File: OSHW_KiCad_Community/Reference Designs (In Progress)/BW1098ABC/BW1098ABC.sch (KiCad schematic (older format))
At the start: 10 parts

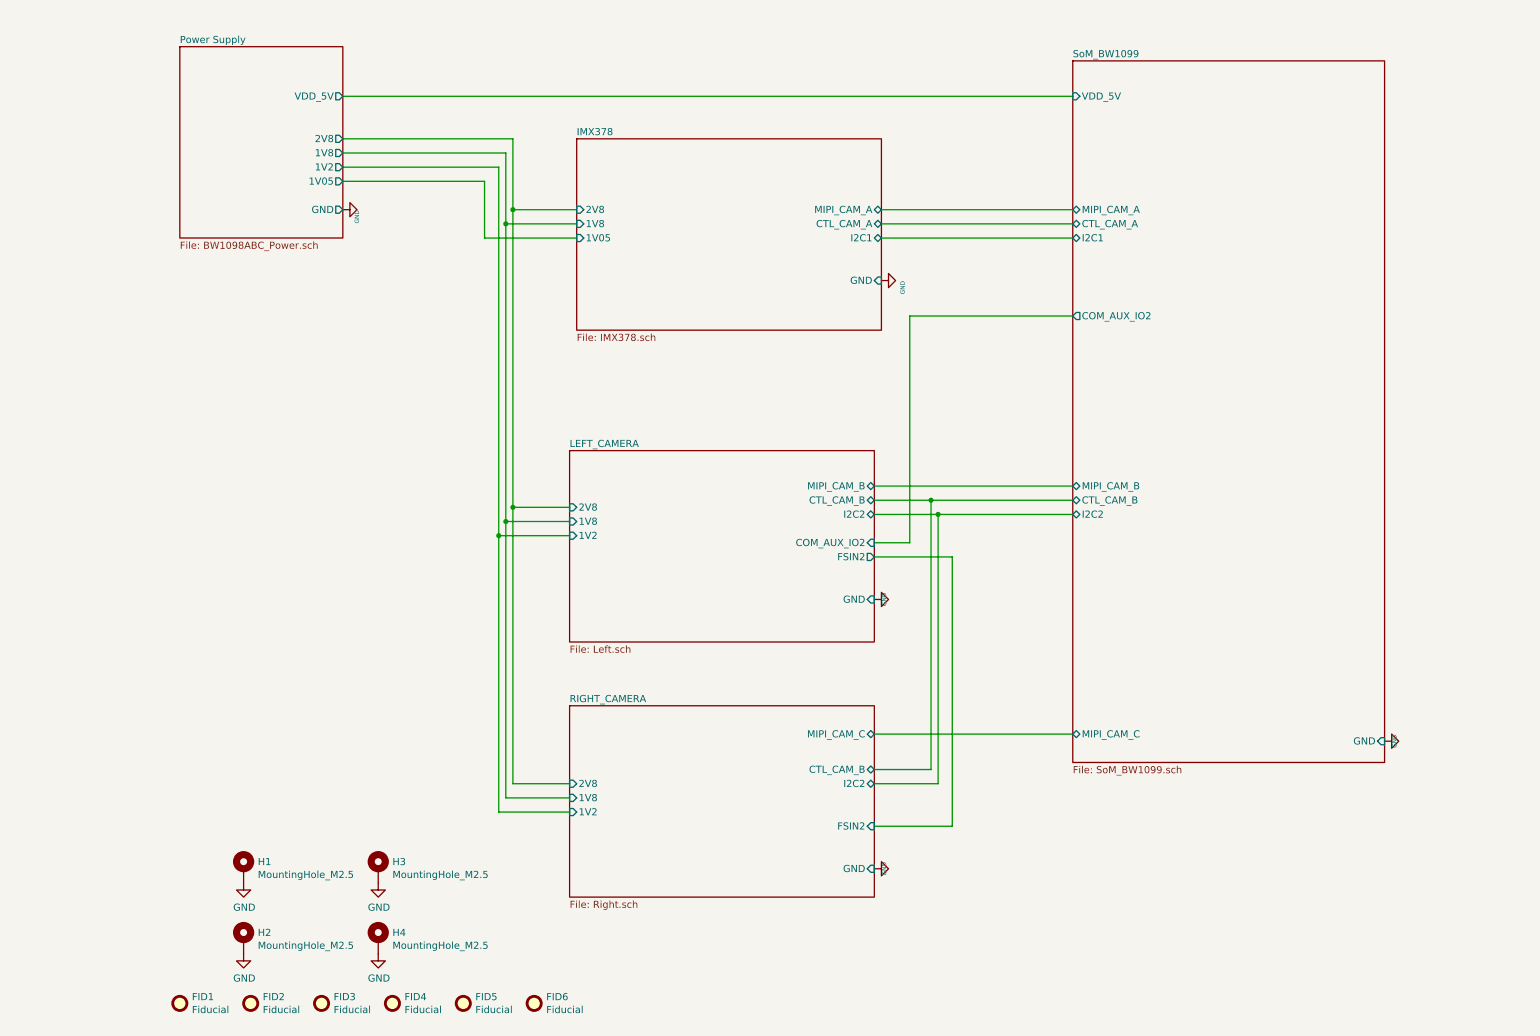
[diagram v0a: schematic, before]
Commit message: BW1098ABC - added back in usbc, got rid of hierarchical labeling in favor of globals. Passes ERC
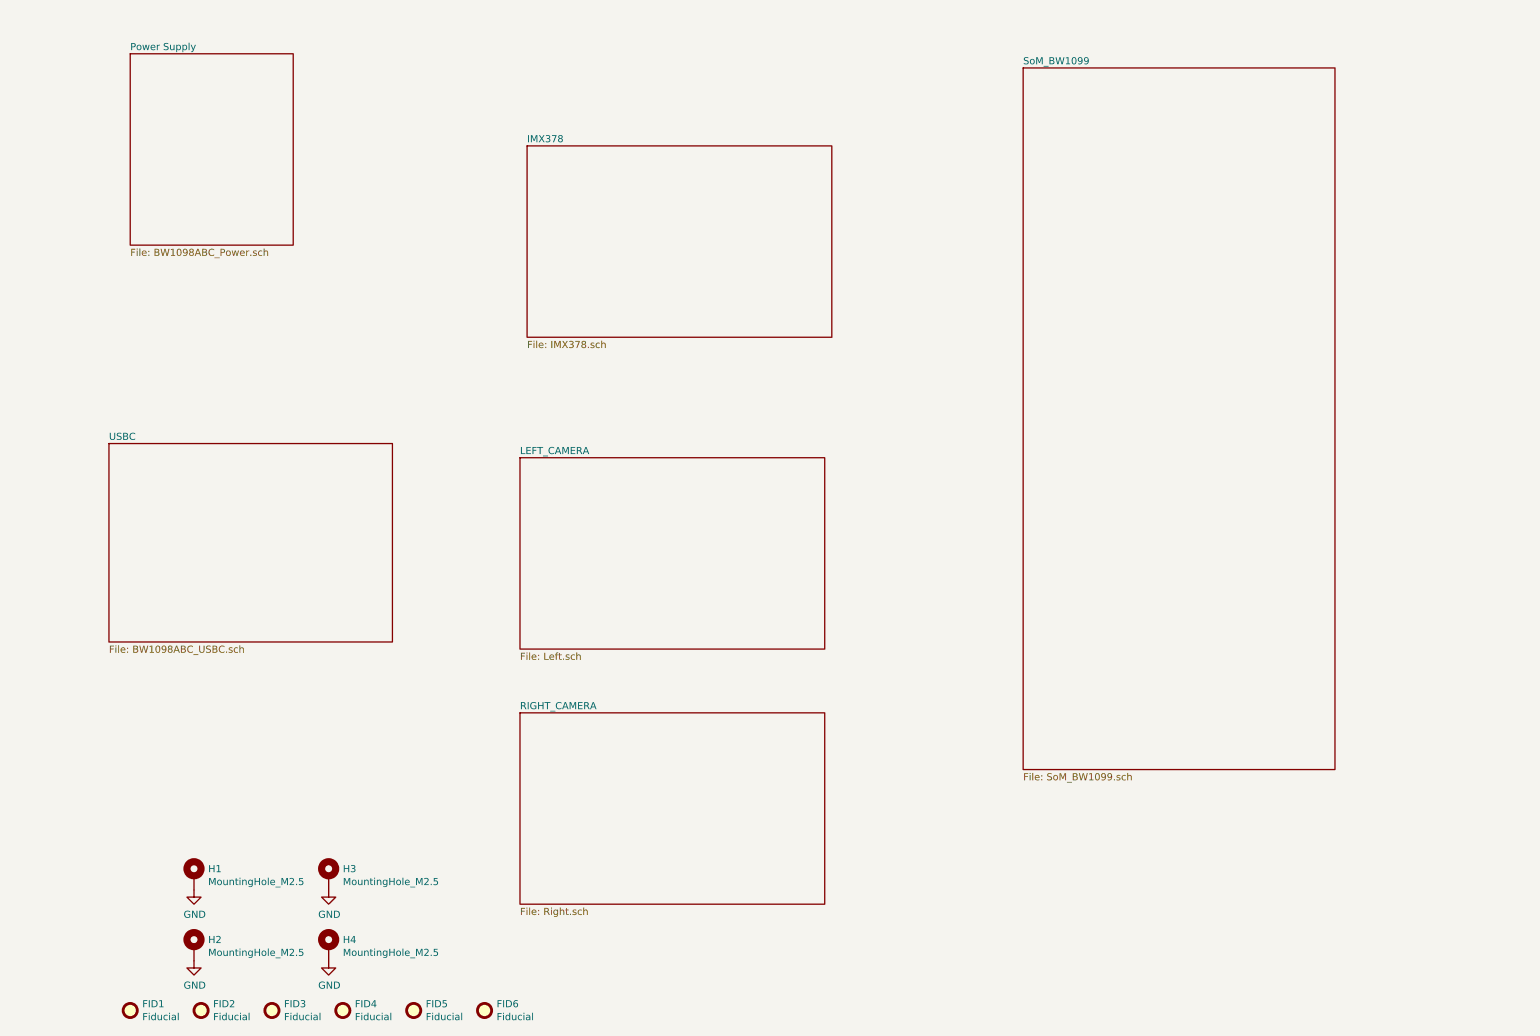
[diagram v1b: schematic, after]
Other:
- moved on the sheet: FID1, FID2, FID3, FID4, FID5

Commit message: going through footprints and datasheet stuff
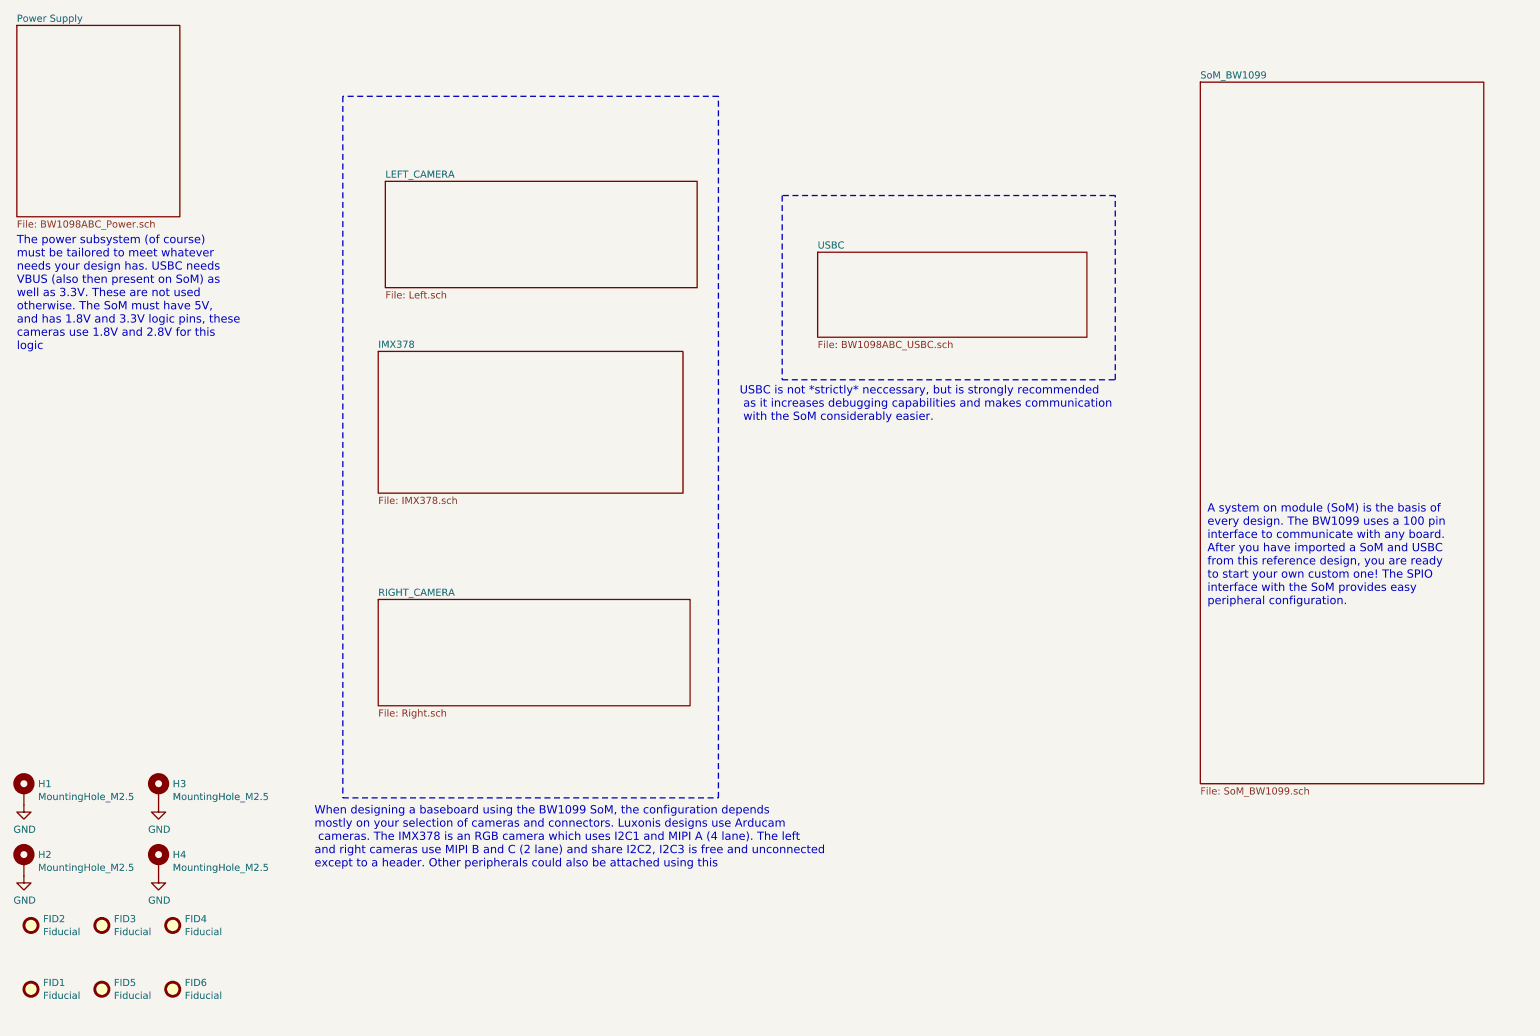
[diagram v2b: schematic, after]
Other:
- note added: "A system on module (SoM) is the basis of \nevery design. The BW1099 uses a 100 pin\ninterface to communicate with any board. \nAfter you have imported a SoM and USBC\nfrom this reference design, you are ready \nto start your own custom one! The SPIO \ninterface with the SoM provides easy \nperipheral configuration."
- note added: "The power subsystem (of course)\nmust be tailored to meet whatever\nneeds your design has. USBC needs\nVBUS (also then present on SoM) as \nwell as 3.3V. These are not used \notherwise. The SoM must have 5V, \nand has 1.8V and 3.3V logic pins, these \ncameras use 1.8V and 2.8V for this \nlogic"
- note added: "USBC is not *strictly* neccessary, but is strongly recommended\n as it increases debugging capabilities and makes communication\n with the SoM considerably easier.\n"
- note added: "When designing a baseboard using the BW1099 SoM, the configuration depends \nmostly on your selection of cameras and connectors. Luxonis designs use Arducam\n cameras. The IMX378 is an RGB camera which uses I2C1 and MIPI A (4 lane). The left \nand right cameras use MIPI B and C (2 lane) and share I2C2, I2C3 is free and unconnected \nexcept to a header. Other peripherals could also be attached usi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"
- moved on the sheet: FID1, FID2, FID3, FID4, FID5, FID6, H1, H2, H3, H4
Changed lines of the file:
@@
 $EndDescr
 $Sheet
-S 7700 900  2200 4950
+S 8950 1000 2000 4950
 U 5FF8D9B2
 F0 "SoM_BW1099" 50
@@
 $EndSheet
 $Sheet
-S 4150 5450 2150 1350
+S 3150 4650 2200 750
 U 5FF8D40A
 F0 "RIGHT_CAMERA" 50
@@
 L Mechanical:Fiducial FID1
 U 1 1 6049A903
-P 1400 7550
-F 0 "FID1" H 1485 7596 50  0000 L CNN
-F 1 "Fiducial" H 1485 7505 50  0000 L CNN
-F 2 "Fiducial:Fiducial_1mm_Mask2mm" H 1400 7550 50  0001 C CNN
-F 3 "~" H 1400 7550 50  0001 C CNN
-	1    1400 7550
+P 700 7400
+F 0 "FID1" H 785 7446 50  0000 L CNN
+F 1 "Fiducial" H 785 7355 50  0000 L CNN
+F 2 "Fiducial:Fiducial_1mm_Mask2mm" H 700 7400 50  0001 C CNN
+F 3 "~" H 700 7400 50  0001 C CNN
+	1    700  7400
 	1    0    0    -1
 $EndComp
@@
 L Mechanical:Fiducial FID2
 U 1 1 5FF51DEB
-P 1900 7550
-F 0 "FID2" H 1985 7596 50  0000 L CNN
-F 1 "Fiducial" H 1985 7505 50  0000 L CNN
-F 2 "Fiducial:Fiducial_1mm_Mask2mm" H 1900 7550 50  0001 C CNN
-F 3 "~" H 1900 7550 50  0001 C CNN
-	1    1900 7550
+P 700 6950
+F 0 "FID2" H 785 6996 50  0000 L CNN
+F 1 "Fiducial" H 785 6905 50  0000 L CNN
+F 2 "Fiducial:Fiducial_1mm_Mask2mm" H 700 6950 50  0001 C CNN
+F 3 "~" H 700 6950 50  0001 C CNN
+	1    700  6950
 	1    0    0    -1
 $EndComp
@@
 L Mechanical:Fiducial FID3
 U 1 1 6049A905
-P 2400 7550
-F 0 "FID3" H 2485 7596 50  0000 L CNN
-F 1 "Fiducial" H 2485 7505 50  0000 L CNN
-F 2 "Fiducial:Fiducial_1mm_Mask2mm" H 2400 7550 50  0001 C CNN
-F 3 "~" H 2400 7550 50  0001 C CNN
-	1    2400 7550
+P 1200 6950
+F 0 "FID3" H 1285 6996 50  0000 L CNN
+F 1 "Fiducial" H 1285 6905 50  0000 L CNN
+F 2 "Fiducial:Fiducial_1mm_Mask2mm" H 1200 6950 50  0001 C CNN
+F 3 "~" H 1200 6950 50  0001 C CNN
+	1    1200 6950
 	1    0    0    -1
 $EndComp
@@
 L Mechanical:Fiducial FID4
 U 1 1 6049A906
-P 2900 7550
-F 0 "FID4" H 2985 7596 50  0000 L CNN
-F 1 "Fiducial" H 2985 7505 50  0000 L CNN
-F 2 "Fiducial:Fiducial_1mm_Mask2mm" H 2900 7550 50  0001 C CNN
-F 3 "~" H 2900 7550 50  0001 C CNN
-	1    2900 7550
+P 1700 6950
+F 0 "FID4" H 1785 6996 50  0000 L CNN
+F 1 "Fiducial" H 1785 6905 50  0000 L CNN
+F 2 "Fiducial:Fiducial_1mm_Mask2mm" H 1700 6950 50  0001 C CNN
+F 3 "~" H 1700 6950 50  0001 C CNN
+	1    1700 6950
 	1    0    0    -1
 $EndComp
@@
 L Mechanical:Fiducial FID5
 U 1 1 6049A907
-P 3400 7550
-F 0 "FID5" H 3485 7596 50  0000 L CNN
-F 1 "Fiducial" H 3485 7505 50  0000 L CNN
-F 2 "Fiducial:Fiducial_1mm_Mask2mm" H 3400 7550 50  0001 C CNN
-F 3 "~" H 3400 7550 50  0001 C CNN
-	1    3400 7550
+P 1200 7400
+F 0 "FID5" H 1285 7446 50  0000 L CNN
+F 1 "Fiducial" H 1285 7355 50  0000 L CNN
+F 2 "Fiducial:Fiducial_1mm_Mask2mm" H 1200 7400 50  0001 C CNN
+F 3 "~" H 1200 7400 50  0001 C CNN
+	1    1200 7400
 	1    0    0    -1
 $EndComp
@@
 L Mechanical:Fiducial FID6
 U 1 1 600C0C22
-P 3900 7550
-F 0 "FID6" H 3985 7596 50  0000 L CNN
-F 1 "Fiducial" H 3985 7505 50  0000 L CNN
-F 2 "Fiducial:Fiducial_1mm_Mask2mm" H 3900 7550 50  0001 C CNN
-F 3 "~" H 3900 7550 50  0001 C CNN
-	1    3900 7550
+P 1700 7400
+F 0 "FID6" H 1785 7446 50  0000 L CNN
+F 1 "Fiducial" H 1785 7355 50  0000 L CNN
+F 2 "Fiducial:Fiducial_1mm_Mask2mm" H 1700 7400 50  0001 C CNN
+F 3 "~" H 1700 7400 50  0001 C CNN
+	1    1700 7400
 	1    0    0    -1
 $EndComp
@@
 L BW1098ABC-rescue:Mechanical_MountingHole_Pad-depthAI_sch H1
 U 1 1 600C0C23
-P 1850 6600
-F 0 "H1" H 1950 6649 50  0000 L CNN
-F 1 "MountingHole_M2.5" H 1950 6558 50  0000 L CNN
-F 2 "fp_luxonis:Mounting_Wuerth_WA-SMSI-M2_H3mm_9774030243" H 1850 6600 50  0001 C CNN
-F 3 "" H 1850 6600 50  0001 C CNN
-	1    1850 6600
+P 650 6000
+F 0 "H1" H 750 6049 50  0000 L CNN
+F 1 "MountingHole_M2.5" H 750 5958 50  0000 L CNN
+F 2 "fp_luxonis:Mounting_Wuerth_WA-SMSI-M2_H3mm_9774030243" H 650 6000 50  0001 C CNN
+F 3 "" H 650 6000 50  0001 C CNN
+	1    650  6000
 	1    0    0    -1
 $EndComp
@@
 L BW1098ABC-rescue:Mechanical_MountingHole_Pad-depthAI_sch H2
 U 1 1 600C0C24
-P 1850 7100
-F 0 "H2" H 1950 7149 50  0000 L CNN
-F 1 "MountingHole_M2.5" H 1950 7058 50  0000 L CNN
-F 2 "fp_luxonis:Mounting_Wuerth_WA-SMSI-M2_H3mm_9774030243" H 1850 7100 50  0001 C CNN
-F 3 "" H 1850 7100 50  0001 C CNN
-	1    1850 7100
+P 650 6500
+F 0 "H2" H 750 6549 50  0000 L CNN
+F 1 "MountingHole_M2.5" H 750 6458 50  0000 L CNN
+F 2 "fp_luxonis:Mounting_Wuerth_WA-SMSI-M2_H3mm_9774030243" H 650 6500 50  0001 C CNN
+F 3 "" H 650 6500 50  0001 C CNN
+	1    650  6500
 	1    0    0    -1
 $EndComp
@@
 L BW1098ABC-rescue:Mechanical_MountingHole_Pad-depthAI_sch H4
 U 1 1 600C0C25
-P 2800 7100
-F 0 "H4" H 2900 7149 50  0000 L CNN
-F 1 "MountingHole_M2.5" H 2900 7058 50  0000 L CNN
-F 2 "fp_luxonis:Mounting_Wuerth_WA-SMSI-M2_H3mm_9774030243" H 2800 7100 50  0001 C CNN
-F 3 "" H 2800 7100 50  0001 C CNN
-	1    2800 7100
+P 1600 6500
+F 0 "H4" H 1700 6549 50  0000 L CNN
+F 1 "MountingHole_M2.5" H 1700 6458 50  0000 L CNN
+F 2 "fp_luxonis:Mounting_Wuerth_WA-SMSI-M2_H3mm_9774030243" H 1600 6500 50  0001 C CNN
+F 3 "" H 1600 6500 50  0001 C CNN
+	1    1600 6500
 	1    0    0    -1
 $EndComp
@@
 L BW1098ABC-rescue:Mechanical_MountingHole_Pad-depthAI_sch H3
 U 1 1 600C0C26
-P 2800 6600
-F 0 "H3" H 2900 6649 50  0000 L CNN
-F 1 "MountingHole_M2.5" H 2900 6558 50  0000 L CNN
-F 2 "fp_luxonis:Mounting_Wuerth_WA-SMSI-M2_H3mm_9774030243" H 2800 6600 50  0001 C CNN
-F 3 "" H 2800 6600 50  0001 C CNN
-	1    2800 6600
-	1    0    0    -1
-$EndComp
-$Sheet
-S 1400 800  1150 1350
+P 1600 6000
+F 0 "H3" H 1700 6049 50  0000 L CNN
+F 1 "MountingHole_M2.5" H 1700 5958 50  0000 L CNN
+F 2 "fp_luxonis:Mounting_Wuerth_WA-SMSI-M2_H3mm_9774030243" H 1600 6000 50  0001 C CNN
+F 3 "" H 1600 6000 50  0001 C CNN
+	1    1600 6000
+	1    0    0    -1
+$EndComp
+$Sheet
+S 600  600  1150 1350
 U 604AEAFA
 F0 "Power Supply" 50
@@
 $EndSheet
 $Sheet
-S 4200 1450 2150 1350
+S 3150 2900 2150 1000
 U 5FF8D4A5
 F0 "IMX378" 50
@@
 $EndSheet
 $Sheet
-S 4150 3650 2150 1350
+S 3200 1700 2200 750
 U 5FF8D2B3
 F0 "LEFT_CAMERA" 50
@@
 L power:GND #PWR0107
 U 1 1 6106C817
-P 1850 6700
-F 0 "#PWR0107" H 1850 6450 50  0001 C CNN
-F 1 "GND" H 1855 6527 50  0000 C CNN
-F 2 "" H 1850 6700 50  0001 C CNN
-F 3 "" H 1850 6700 50  0001 C CNN
-	1    1850 6700
+P 650 6100
+F 0 "#PWR0107" H 650 5850 50  0001 C CNN
+F 1 "GND" H 655 5927 50  0000 C CNN
+F 2 "" H 650 6100 50  0001 C CNN
+F 3 "" H 650 6100 50  0001 C CNN
+	1    650  6100
 	1    0    0    -1
 $EndComp
@@
 L power:GND #PWR0108
 U 1 1 6106D903
-P 2800 6700
-F 0 "#PWR0108" H 2800 6450 50  0001 C CNN
-F 1 "GND" H 2805 6527 50  0000 C CNN
-F 2 "" H 2800 6700 50  0001 C CNN
-F 3 "" H 2800 6700 50  0001 C CNN
-	1    2800 6700
+P 1600 6100
+F 0 "#PWR0108" H 1600 5850 50  0001 C CNN
+F 1 "GND" H 1605 5927 50  0000 C CNN
+F 2 "" H 1600 6100 50  0001 C CNN
+F 3 "" H 1600 6100 50  0001 C CNN
+	1    1600 6100
 	1    0    0    -1
 $EndComp
@@
 L power:GND #PWR0109
 U 1 1 6106E6FC
-P 2800 7200
-F 0 "#PWR0109" H 2800 6950 50  0001 C CNN
-F 1 "GND" H 2805 7027 50  0000 C CNN
-F 2 "" H 2800 7200 50  0001 C CNN
-F 3 "" H 2800 7200 50  0001 C CNN
-	1    2800 7200
+P 1600 6600
+F 0 "#PWR0109" H 1600 6350 50  0001 C CNN
+F 1 "GND" H 1605 6427 50  0000 C CNN
+F 2 "" H 1600 6600 50  0001 C CNN
+F 3 "" H 1600 6600 50  0001 C CNN
+	1    1600 6600
 	1    0    0    -1
 $EndComp
@@
 L power:GND #PWR0110
 U 1 1 6106EA7D
-P 1850 7200
-F 0 "#PWR0110" H 1850 6950 50  0001 C CNN
-F 1 "GND" H 1855 7027 50  0000 C CNN
-F 2 "" H 1850 7200 50  0001 C CNN
-F 3 "" H 1850 7200 50  0001 C CNN
-	1    1850 7200
-	1    0    0    -1
-$EndComp
-$Sheet
-S 1250 3550 2000 1400
+P 650 6600
+F 0 "#PWR0110" H 650 6350 50  0001 C CNN
+F 1 "GND" H 655 6427 50  0000 C CNN
+F 2 "" H 650 6600 50  0001 C CNN
+F 3 "" H 650 6600 50  0001 C CNN
+	1    650  6600
+	1    0    0    -1
+$EndComp
+$Sheet
+S 6250 2200 1900 600
 U 60483E6B
 F0 "USBC" 50
 F1 "BW1098ABC_USBC.sch" 50
 $EndSheet
+Wire Notes Line
+	5550 1100 2900 1100
+Wire Notes Line
+	2900 1100 2900 6050
+Wire Notes Line
+	2900 6050 5550 6050
+Wire Notes Line
+	5550 6050 5550 1100
+Text Notes 2700 6550 0    58   ~ 0
+When designing a baseboard using the BW1099 SoM, the configuration depends \nmostly on your selection of cameras and connectors. Luxonis designs use Arducam\n cameras. The IMX378 is an RGB camera which uses I2C1 and MIPI A (4 lane). The left \nand right cameras use MIPI B and C (2 lane) and share I2C2, I2C3 is free and unconnected \nexcept to a header. Other peripherals could also be attached using this\n
+Wire Notes Line
+	8350 1800 6000 1800
+Wire Notes Line
+	6000 1800 6000 3100
+Wire Notes Line
+	6000 3100 8350 3100
+Wire Notes Line
+	8350 3100 8350 1800
+Text Notes 5700 3400 0    58   ~ 0
+USBC is not *strictly* neccessary, but is strongly recommended\n as it increases debugging capabilities and makes communication\n with the SoM considerably easier.\n
+Text Notes 9000 4700 0    58   ~ 0
+A system on module (SoM) is the basis of \nevery design. The BW1099 uses a 100 pin\ninterface to communicate with any board. \nAfter you have imported a SoM and USBC\nfrom this reference design, you are ready \nto start your own custom one! The SPIO \ninterface with the SoM provides easy \nperipheral configuration.
+Text Notes 600  2900 0    58   ~ 0
+The power subsystem (of course)\nmust be tailored to meet whatever\nneeds your design has. USBC needs\nVBUS (also then present on SoM) as \nwell as 3.3V. These are not used \notherwise. The SoM must have 5V, \nand has 1.8V and 3.3V logic pins, these \ncameras use 1.8V and 2.8V for this \nlogic
 $EndSCHEMATC

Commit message: both camera connector footprints completed
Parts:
- H1, H2, H3, H4: footprint fp_luxonis:Mounting_Wuerth_WA-SMSI-M2_H3mm_9774030243 -> Mounting_Wuerth:Mounting_Wuerth_WA-SMSI-M2_H3mm_9774030243
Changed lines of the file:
@@
 F 0 "H1" H 750 6049 50  0000 L CNN
 F 1 "MountingHole_M2.5" H 750 5958 50  0000 L CNN
-F 2 "fp_luxonis:Mounting_Wuerth_WA-SMSI-M2_H3mm_9774030243" H 650 6000 50  0001 C CNN
+F 2 "Mounting_Wuerth:Mounting_Wuerth_WA-SMSI-M2_H3mm_9774030243" H 650 6000 50  0001 C CNN
 F 3 "" H 650 6000 50  0001 C CNN
 	1    650  6000
@@
 F 0 "H2" H 750 6549 50  0000 L CNN
 F 1 "MountingHole_M2.5" H 750 6458 50  0000 L CNN
-F 2 "fp_luxonis:Mounting_Wuerth_WA-SMSI-M2_H3mm_9774030243" H 650 6500 50  0001 C CNN
+F 2 "Mounting_Wuerth:Mounting_Wuerth_WA-SMSI-M2_H3mm_9774030243" H 650 6500 50  0001 C CNN
 F 3 "" H 650 6500 50  0001 C CNN
 	1    650  6500
@@
 F 0 "H4" H 1700 6549 50  0000 L CNN
 F 1 "MountingHole_M2.5" H 1700 6458 50  0000 L CNN
-F 2 "fp_luxonis:Mounting_Wuerth_WA-SMSI-M2_H3mm_9774030243" H 1600 6500 50  0001 C CNN
+F 2 "Mounting_Wuerth:Mounting_Wuerth_WA-SMSI-M2_H3mm_9774030243" H 1600 6500 50  0001 C CNN
 F 3 "" H 1600 6500 50  0001 C CNN
 	1    1600 6500
@@
 F 0 "H3" H 1700 6049 50  0000 L CNN
 F 1 "MountingHole_M2.5" H 1700 5958 50  0000 L CNN
-F 2 "fp_luxonis:Mounting_Wuerth_WA-SMSI-M2_H3mm_9774030243" H 1600 6000 50  0001 C CNN
+F 2 "Mounting_Wuerth:Mounting_Wuerth_WA-SMSI-M2_H3mm_9774030243" H 1600 6000 50  0001 C CNN
 F 3 "" H 1600 6000 50  0001 C CNN
 	1    1600 6000
